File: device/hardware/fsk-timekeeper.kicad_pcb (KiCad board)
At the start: 2 copper layers, 92 x 57 mm, 27 parts, among them J1 SENSOR BA2M-DDT, SW1 POWER, U1 SuperMini nRF52840, U2 Ai-Thinker Ra-01SH, U3 TPS61040DBV, U4 ATGM336H

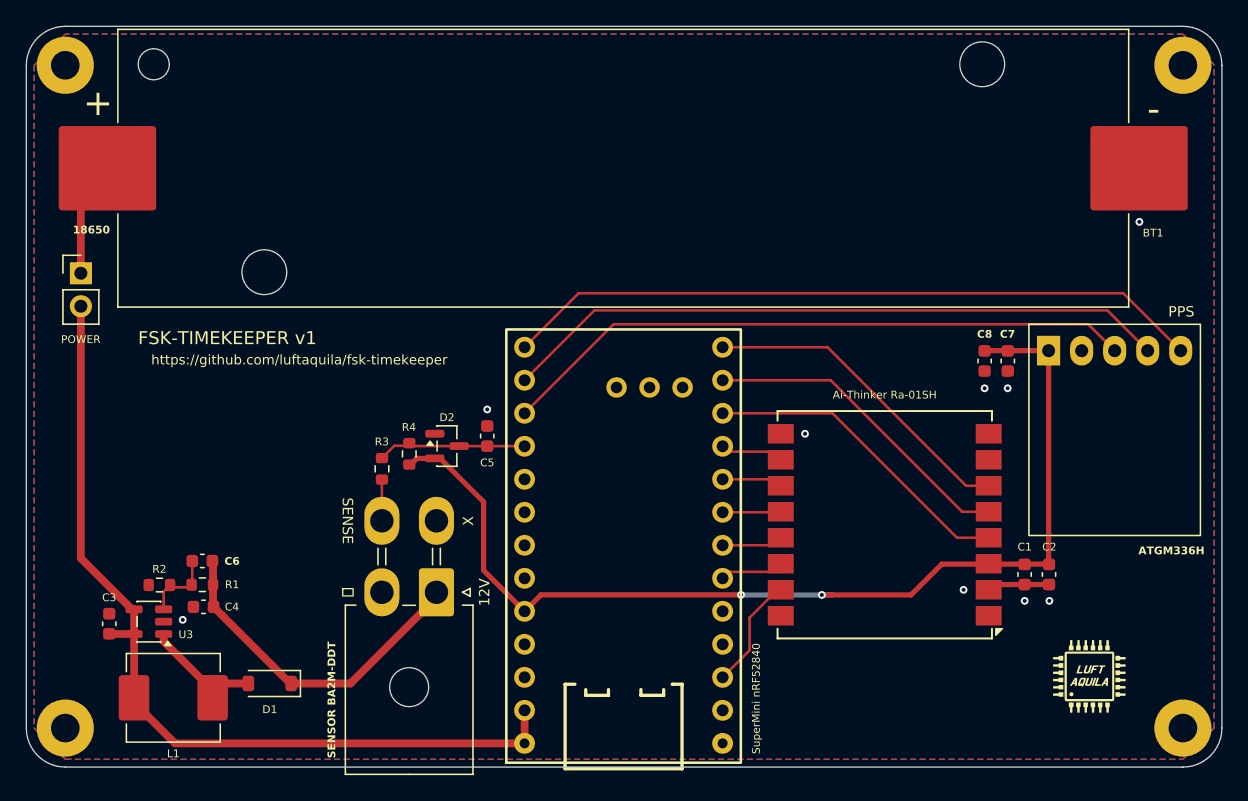
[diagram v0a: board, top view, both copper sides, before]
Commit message: fix: leave the Ra-01SH TXEN and RXEN pins unconnected
The Ra-01SH ties TXEN to the SX1262 DIO2 through a 0 ohm resistor and
leaves RXEN open, and RadioLib's begin() already makes DIO2 drive the RF
switch. Driving TXEN from P1.04 fought DIO2 at the start and end of every
transmission, and RXEN reached nothing. The schematic and board drop both
nets, and the firmware drops setRfSwitchPins() and the pin definitions.

The board also carries the refilled GND zone, the bottom +BATT trace
moved to y = 125 mm, and the J1 and SW1 values synced from the schematic.

Co-Authored-By: Claude Opus 5.5 <noreply@anthropic.com>
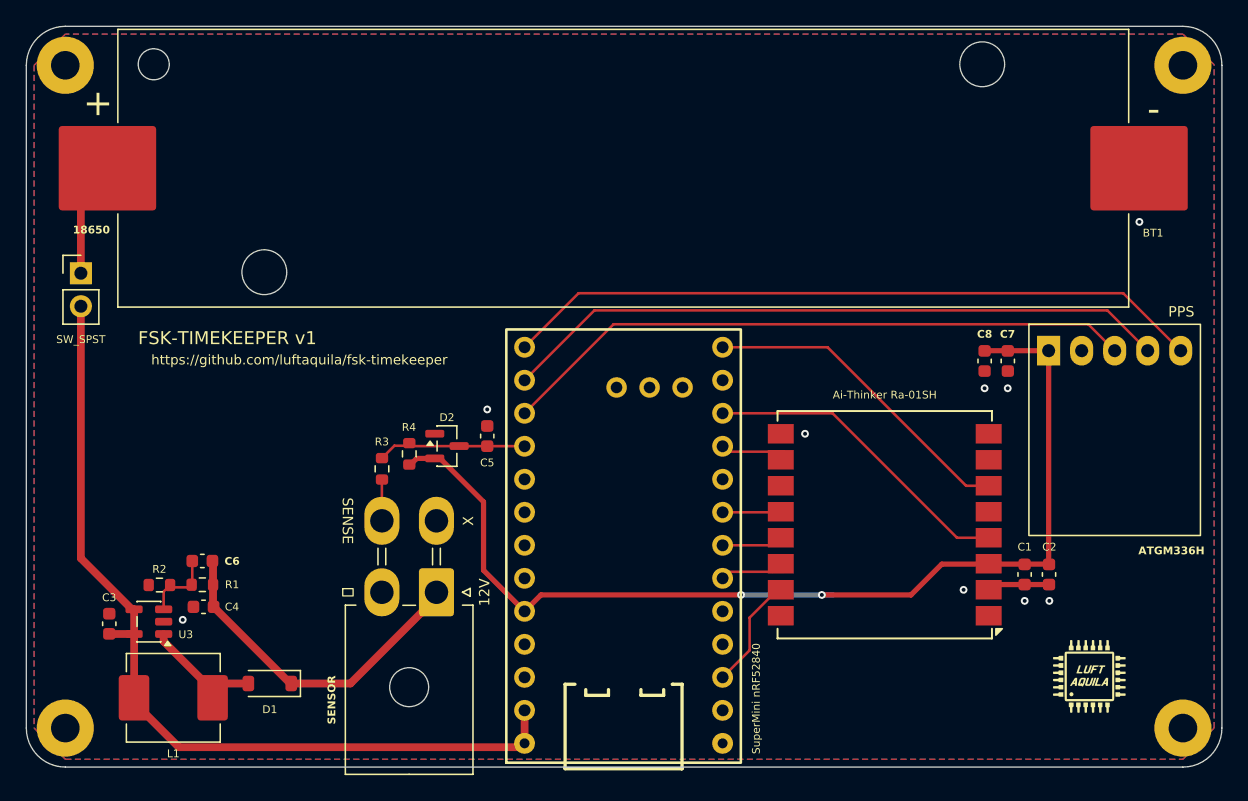
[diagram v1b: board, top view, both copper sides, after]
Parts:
- J1: value SENSOR BA2M-DDT -> SENSOR
- SW1: value POWER -> SW_SPST
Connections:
- U1 pad 11: /TXEN -> unconnected-(U1-P1.04-LF-Pad11)
- U1 pad 8: /RXEN -> unconnected-(U1-P0.24-Pad8)
- U2 pad 11: /RXEN -> unconnected-(U2-DIO5-Pad11)
- U2 pad 5: /TXEN -> unconnected-(U2-DIO0-Pad5)
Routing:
- net /TXEN: track 24.7 -> 0.00 mm
- net /RXEN: track 5.57 -> 0.00 mm
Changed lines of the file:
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@@
 			)
 		)
-		(property "Value" "POWER"
+		(property "Value" "SW_SPST"
 			(at -0.0056 5.0944 0)
 			(layer "F.SilkS")
@@
 			)
 		)
-		(property "Value" "SENSOR BA2M-DDT"
+		(property "Value" "SENSOR"
 			(at 8.0608 -8.2804 90)
 			(layer "F.SilkS")
@@
 			(layers "*.Cu" "*.Mask")
 			(remove_unused_layers no)
-			(net "/RXEN")
+			(net "unconnected-(U1-P0.24-Pad8)")
 			(pinfunction "P0.24_8")
-			(pintype "bidirectional")
+			(pintype "bidirectional+no_connect")
 		)
 		(pad "9" thru_hole circle
@@
 			(layers "*.Cu" "*.Mask")
 			(remove_unused_layers no)
-			(net "/TXEN")
+			(net "unconnected-(U1-P1.04-LF-Pad11)")
 			(pinfunction "P1.04-LF_11")
-			(pintype "bidirectional")
+			(pintype "bidirectional+no_connect")
 		)
 		(pad "12" thru_hole circle
@@
 			(size 2 1.5)
 			(layers "F.Cu" "F.Mask" "F.Paste")
-			(net "/TXEN")
+			(net "unconnected-(U2-DIO0-Pad5)")
 			(pinfunction "DIO0_5")
-			(pintype "bidirectional")
+			(pintype "bidirectional+no_connect")
 		)
 		(pad "6" smd rect
@@
 			(size 2 1.5)
 			(layers "F.Cu" "F.Mask" "F.Paste")
-			(net "/RXEN")
+			(net "unconnected-(U2-DIO5-Pad11)")
 			(pinfunction "DIO5_11")
-			(pintype "bidirectional")
+			(pintype "bidirectional+no_connect")
 		)
 		(pad "12" smd rect
@@
 	)
 	(segment
-		(start 109.4579 116.2916)
-		(end 109.4579 114.3916)
+		(start 109.45 121.2)
+		(end 109.45 121.55)
 		(width 0.6)
 		(layer "F.Cu")
@@
 	)
 	(segment
-		(start 112.604958 124.704958)
-		(end 139.504 124.704958)
+		(start 109.4579 116.2916)
+		(end 109.4579 114.3916)
 		(width 0.6)
 		(layer "F.Cu")
@@
 	)
 	(segment
+		(start 112.9 125)
+		(end 139.208958 125)
+		(width 0.6)
+		(layer "F.Cu")
+		(net "+BATT")
+	)
+	(segment
 		(start 105.3648 110.4648)
 		(end 105.3648 91.07)
@@
 	)
 	(segment
-		(start 109.45 121.55)
-		(end 112.604958 124.704958)
+		(start 139.208958 125)
+		(end 139.504 124.704958)
 		(width 0.6)
 		(layer "F.Cu")
@@
 	)
 	(segment
-		(start 109.45 121.2)
-		(end 109.45 121.55)
+		(start 109.45 121.55)
+		(end 112.9 125)
 		(width 0.6)
 		(layer "F.Cu")
@@
 	)
 	(segment
-		(start 105.3648 88.53)
-		(end 105.3648 82.4952)
-		(width 0.6)
-		(layer "F.Cu")
-		(net "Net-(BT1-+)")
-	)
-	(segment
-		(start 105.3648 82.4952)
-		(end 107.41 80.45)
-		(width 0.2)
-		(layer "F.Cu")
-		(net "Net-(BT1-+)")
-	)
-	(segment
 		(start 136.3472 106.1212)
 		(end 133.005842 102.779842)
@@
 	)
 	(segment
+		(start 182.879 92.456)
+		(end 146.352958 92.456)
+		(width 0.2)
+		(layer "F.Cu")
+		(net "/RX")
+	)
+	(segment
+		(start 146.352958 92.456)
+		(end 139.504 99.304958)
+		(width 0.2)
+		(layer "F.Cu")
+		(net "/RX")
+	)
+	(segment
+		(start 184.912 94.489)
+		(end 182.879 92.456)
+		(width 0.2)
+		(layer "F.Cu")
+		(net "/RX")
+	)
+	(segment
+		(start 187.452 94.489)
+		(end 184.3522 91.3892)
+		(width 0.2)
+		(layer "F.Cu")
+		(net "/TX")
+	)
+	(segment
+		(start 184.3522 91.3892)
+		(end 144.879758 91.3892)
+		(width 0.2)
+		(layer "F.Cu")
+		(net "/TX")
+	)
+	(segment
+		(start 144.879758 91.3892)
+		(end 139.504 96.764958)
+		(width 0.2)
+		(layer "F.Cu")
+		(net "/TX")
+	)
+	(segment
+		(start 189.992 94.489)
+		(end 185.5714 90.0684)
+		(width 0.2)
+		(layer "F.Cu")
+		(net "/PPS")
+	)
+	(segment
+		(start 185.5714 90.0684)
+		(end 143.660558 90.0684)
+		(width 0.2)
+		(layer "F.Cu")
+		(net "/PPS")
+	)
+	(segment
+		(start 143.660558 90.0684)
+		(end 139.504 94.224958)
+		(width 0.2)
+		(layer "F.Cu")
+		(net "/PPS")
+	)
+	(segment
+		(start 105.3648 88.53)
+		(end 105.3648 82.4952)
+		(width 0.6)
+		(layer "F.Cu")
+		(net "Net-(BT1-+)")
+	)
+	(segment
+		(start 105.3648 82.4952)
+		(end 107.41 80.45)
+		(width 0.2)
+		(layer "F.Cu")
+		(net "Net-(BT1-+)")
+	)
+	(segment
 		(start 115.575 114.2)
 		(end 121.475 120.1)
@@
 	)
 	(segment
-		(start 154.74401 104.384948)
-		(end 159.612999 104.384948)
-		(width 0.2)
-		(layer "F.Cu")
-		(net "/RXEN")
-	)
-	(segment
-		(start 158.720324 104.384948)
-		(end 159.219376 104.884)
-		(width 0.2)
-		(layer "F.Cu")
-		(net "/RXEN")
-	)
-	(segment
 		(start 154.74401 101.844948)
 		(end 155.159462 102.2604)
@@
 	)
 	(segment
-		(start 175.219376 106.884)
-		(end 173.178525 106.884)
-		(width 0.2)
-		(layer "F.Cu")
-		(net "/TXEN")
-	)
-	(segment
-		(start 173.178525 106.884)
-		(end 163.059473 96.764948)
-		(width 0.2)
-		(layer "F.Cu")
-		(net "/TXEN")
-	)
-	(segment
-		(start 163.059473 96.764948)
-		(end 154.74401 96.764948)
-		(width 0.2)
-		(layer "F.Cu")
-		(net "/TXEN")
-	)
-	(segment
 		(start 173.478525 104.884)
 		(end 162.819473 94.224948)
@@
 		(net "Net-(U3-FB)")
 	)
-	(segment
-		(start 189.992 94.489)
-		(end 185.5714 90.0684)
-		(width 0.2)
-		(layer "F.Cu")
-		(net "/PPS")
-	)
-	(segment
-		(start 185.5714 90.0684)
-		(end 143.660558 90.0684)
-		(width 0.2)
-		(layer "F.Cu")
-		(net "/PPS")
-	)
-	(segment
-		(start 143.660558 90.0684)
-		(end 139.504 94.224958)
-		(width 0.2)
-		(layer "F.Cu")
-		(net "/PPS")
-	)
-	(segment
-		(start 187.452 94.489)
-		(end 184.3522 91.3892)
-		(width 0.2)
-		(layer "F.Cu")
-		(net "/TX")
-	)
-	(segment
-		(start 184.3522 91.3892)
-		(end 144.879758 91.3892)
-		(width 0.2)
-		(layer "F.Cu")
-		(net "/TX")
-	)
-	(segment
-		(start 144.879758 91.3892)
-		(end 139.504 96.764958)
-		(width 0.2)
-		(layer "F.Cu")
-		(net "/TX")
-	)
-	(segment
-		(start 182.879 92.456)
-		(end 146.352958 92.456)
-		(width 0.2)
-		(layer "F.Cu")
-		(net "/RX")
-	)
-	(segment
-		(start 146.352958 92.456)
-		(end 139.504 99.304958)
-		(width 0.2)
-		(layer "F.Cu")
-		(net "/RX")
-	)
-	(segment
-		(start 184.912 94.489)
-		(end 182.879 92.456)
-		(width 0.2)
-		(layer "F.Cu")
-		(net "/RX")
-	)
 	(zone

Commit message: add: stitch the GND pours with vias
The top and bottom GND pours were joined by only nine vias and the
through-hole pads. GND vias now run along the board edge, around the
Ra-01SH, on a roughly 10 mm grid, and beside the ground pads of C3, R2,
D2, U2 pin 16, U4 pin 2 and the battery negative, for 69 in total. The
via by U3 and the one by C4 are merged into one. The +3.3V B.Cu stub past
its via is trimmed and the zones are refilled.

Co-Authored-By: Claude Opus 5.5 <noreply@anthropic.com>
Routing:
- net +3.3V: track 81.4 -> 80.5 mm
- net GND: vias 9 -> 69
